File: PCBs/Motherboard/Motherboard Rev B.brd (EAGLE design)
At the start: 95.9 x 90.2 mm, 52 parts, among them J2 MOLEX_504050-0491, Q1 32kHZ, U1 Value, X1 2514-5

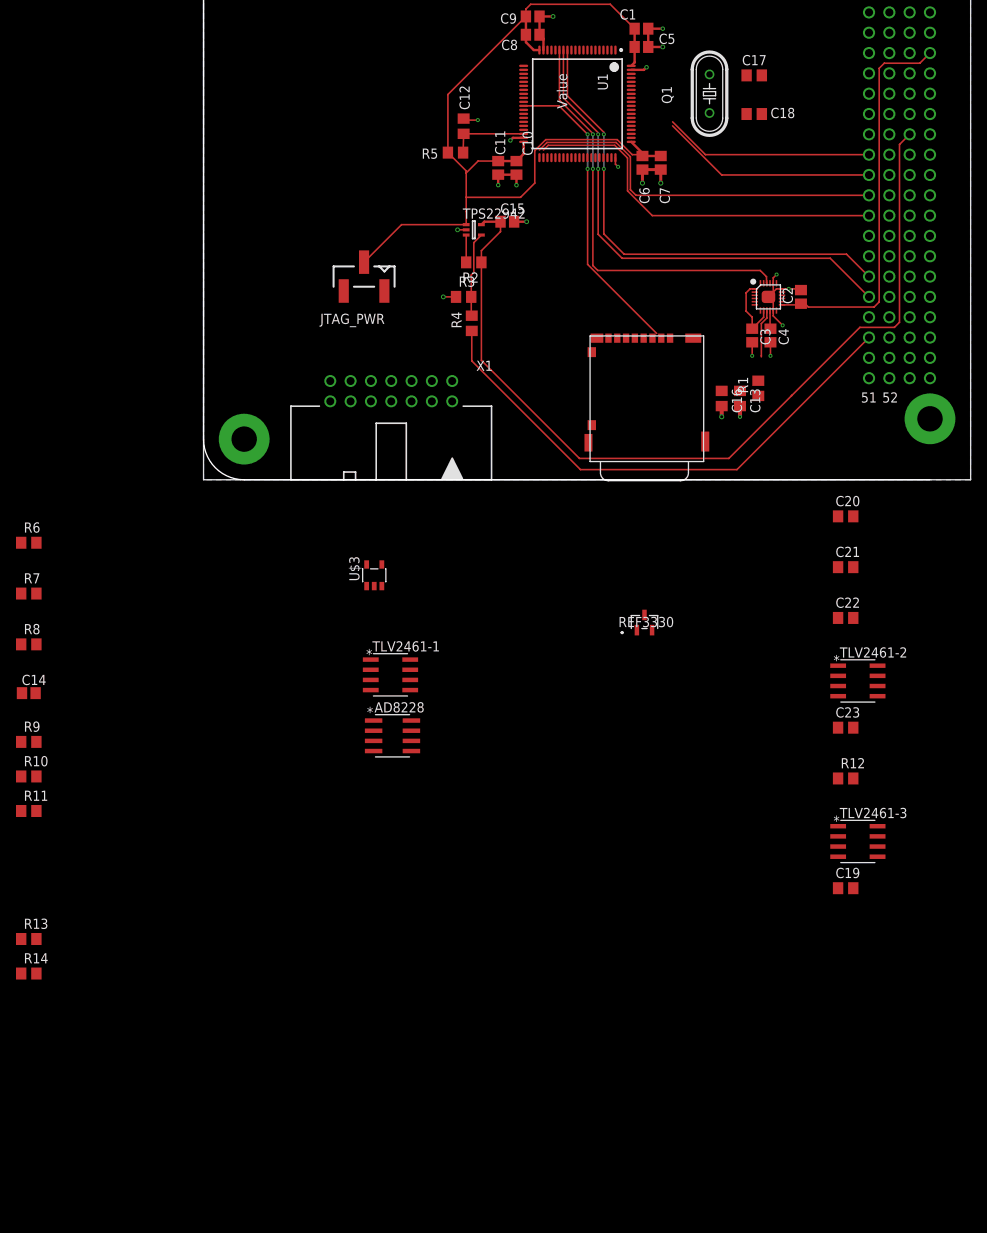
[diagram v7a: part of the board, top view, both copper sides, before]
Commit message: Add HFXtal
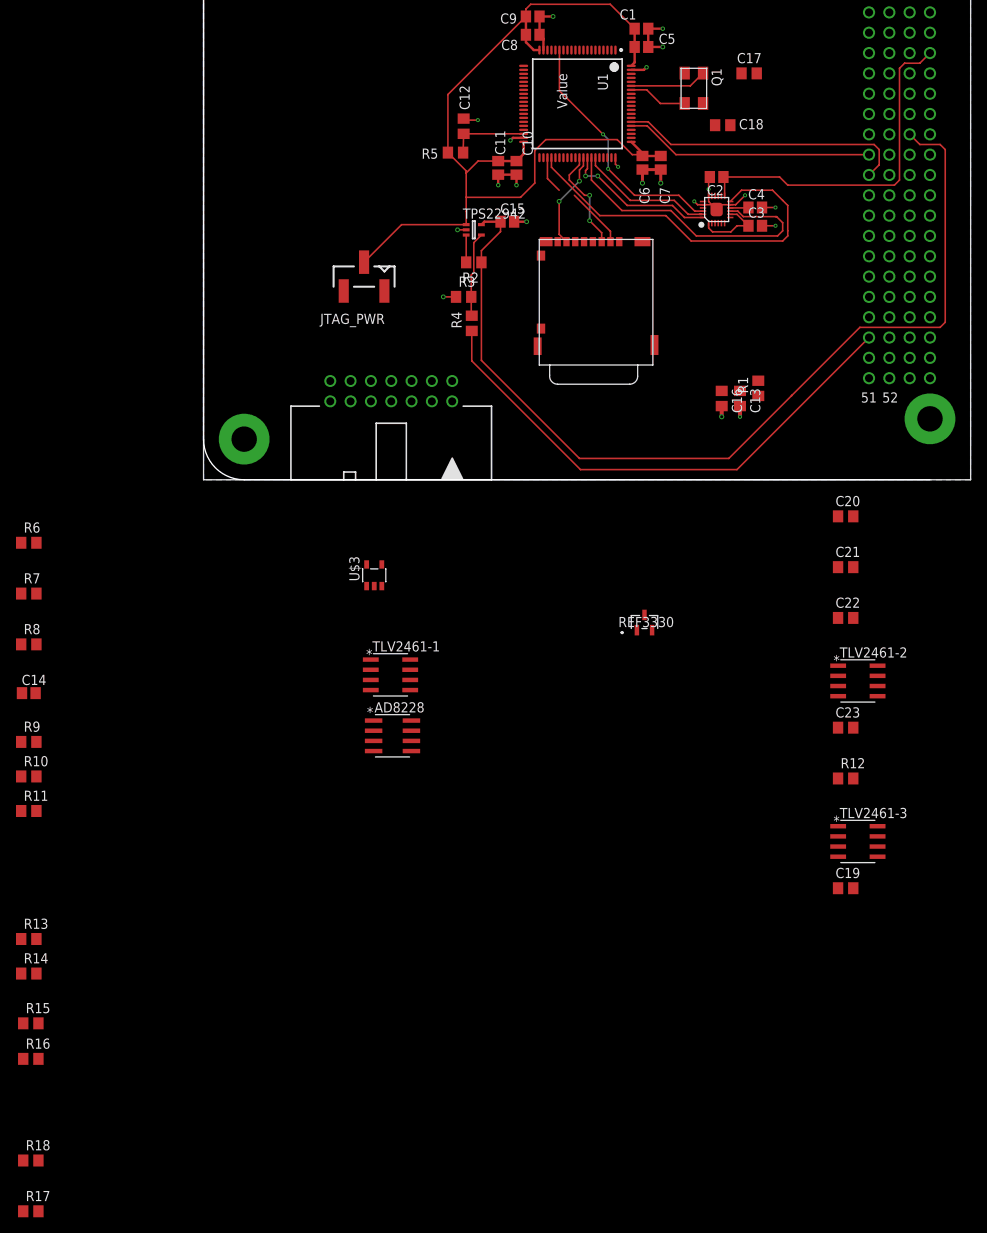
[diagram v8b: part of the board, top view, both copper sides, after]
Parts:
- added R15, R16, R17, R18: 0, resistor:R0805
- C17, C18: value 6pF -> 35pF
- Q1: value 32kHZ -> 16MHz; device crystal:HC49/S -> C5BQ:5X3.2
- moved C2 18.3 mm to (64.1, 37.8), turned to 180 degrees
- moved C4 16.1 mm to (69.0, 34.0), turned to 0 degrees
- moved C3 13.7 mm to (69.0, 31.8), turned to 0 degrees
- moved SD_CONN 13.6 mm to (56.9, 30.3)
- moved U$2 12.7 mm to (64.1, 33.8), turned to 90 degrees
- moved Q1 4.77 mm to (59.7, 51.4), turned to 270 degrees
- moved C18 4.18 mm to (64.9, 44.3)
- moved C17 0.68 mm to (68.2, 50.8)
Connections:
- new net N$12: C18.1, Q1.2, U1.74
- new net N$13: R17.2, TLV2461-3.3
- new net N$14: AD8228.1, AD8228.7, R10.2, R11.1, R15.1, TLV2461-2.3
- new net N$16: R18.1, TLV2461-3.2, TLV2461-3.6
- net N$4: now also Q1.1, U1.75; no longer Q1.2, U1.78
- net N$6: now also AD8228.4, R16.1; no longer C18.1, Q1.1, U1.77
- net STRAIN_OUT: now also R15.2, R18.2; no longer AD8228.1, AD8228.7, R10.2, R11.1, TLV2461-2.3
- net STRN: now also R12.2, R16.2, R17.1; no longer AD8228.4
- net TEMP: no longer R12.2, TLV2461-3.3
- net TEMP_OUT: no longer TLV2461-3.2, TLV2461-3.6
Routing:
- net SCL_EPS: track 61.9 -> 0.00 mm, vias 2 -> 0
- net SDA_EPS: track 60.2 -> 0.00 mm, vias 2 -> 0
- net INT_IMU: track 0.00 -> 47.2 mm
- net PINAVL1_RX: track 47.0 -> 0.00 mm
- net PINAVL1_TX: track 46.7 -> 0.00 mm
- net MISO_IMU: track 6.08 -> 38.0 mm
- net CS_SD: track 37.9 -> 7.66 mm, vias 2 -> 0
- net CS_IMU: track 51.8 -> 31.4 mm
- net MOSI_IMU: track 0.00 -> 19.2 mm, vias 0 -> 2
- net CLK_IMU: track 0.00 -> 17.2 mm
- net MOSI_SD: track 0.00 -> 13.1 mm, vias 0 -> 2
- net MISO_SD: track 0.00 -> 12.1 mm, vias 0 -> 2
- net N$4: track 0.00 -> 9.64 mm
- net LITHIUM_TX: track 27.1 -> 36.1 mm
- net 3V3: track 109.4 -> 117.9 mm
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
